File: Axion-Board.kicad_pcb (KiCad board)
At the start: 2 copper layers, 84 x 54.5 mm, 79 parts, among them J1 USB_C_Receptacle_USB2.0, J14 QE2B, J15 RGB2, J16 RGB1, J17 QE1, J18 QE2, J19 USB Header, J2 SWD, J20 PS2 Header, J21 QE2A, J3 QE1A, J4 QE1B, J6 GPIO, J7 GPIO, Q1 BSS138, Q10 BSS138, Q11 BSS138, Q2 BSS138, Q3 BSS138, Q4 BSS138, Q5 BSS138, Q6 BSS138, Q7 BSS138, Q8 BSS138, Q9 BSS138, SW1 SW_Push, U1 W25Q128JVS, U2 USBLC6-2SC6, U3 RP2040, U4 XC6206PxxxMR-Regulator_Linear, U5 SN74HCT125DR, U6 78M05_TO252-3, Y1 12MHz

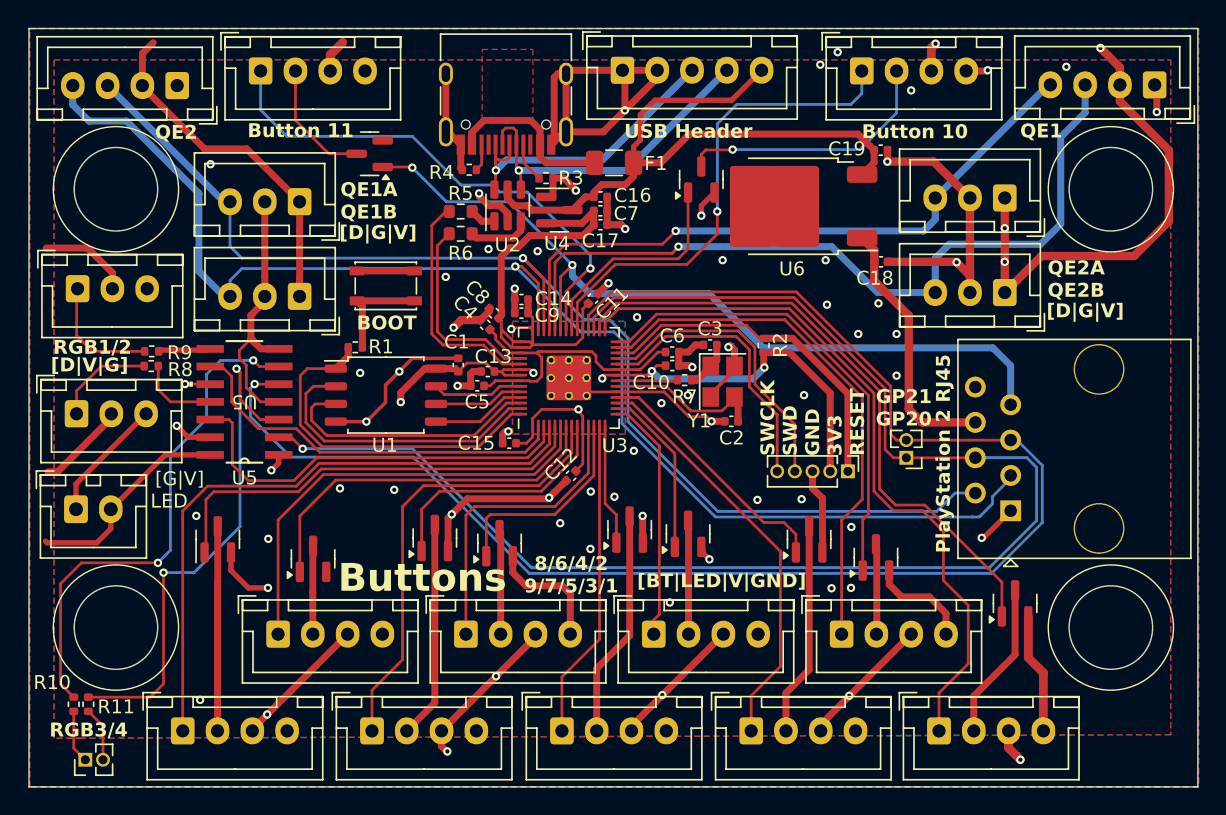
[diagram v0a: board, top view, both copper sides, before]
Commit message: Updated PCB
Changed Edge Cuts holes to mounting hole footprints, and updated track routing to avoid mounting hole courtyards
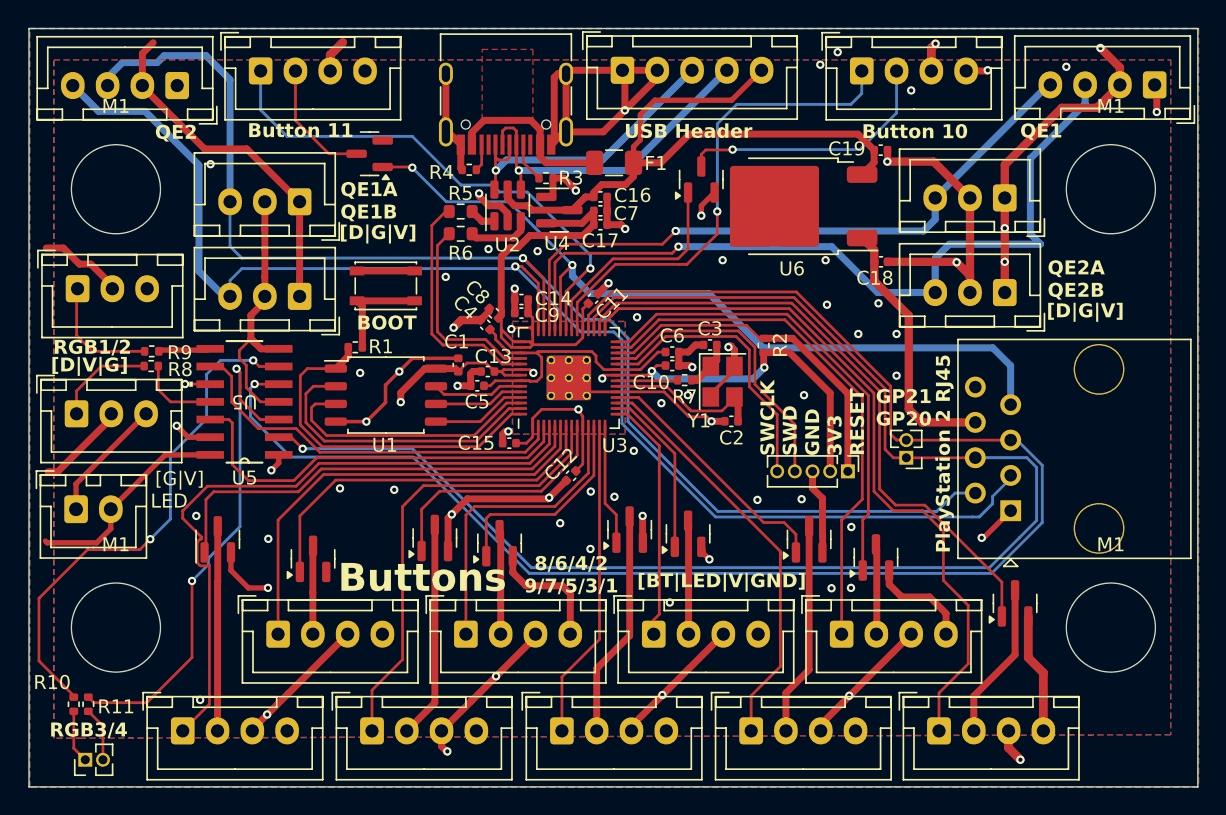
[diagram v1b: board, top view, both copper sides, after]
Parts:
- added M1: MountingHole_6.4mm_M6_ISO14580, MountingHole:MountingHole_6.4mm_M6_ISO14580, F.Cu at (177.7, 63.8)
- added M1: MountingHole_6.4mm_M6_ISO14580, MountingHole:MountingHole_6.4mm_M6_ISO14580, F.Cu at (177.7, 95.3)
- added M1: MountingHole_6.4mm_M6_ISO14580, MountingHole:MountingHole_6.4mm_M6_ISO14580, F.Cu at (106.2, 63.8)
- added M1: MountingHole_6.4mm_M6_ISO14580, MountingHole:MountingHole_6.4mm_M6_ISO14580, F.Cu at (106.2, 95.3)
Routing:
- net VBUS: track 148.9 -> 136.2 mm
- net /PS2CLK: track 86.9 -> 94.2 mm
- net /BT8: track 45.5 -> 47.8 mm
- net Net-(U5-1Y): track 37.8 -> 36.9 mm
- net /QE1A: track 57.4 -> 58.0 mm
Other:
- outline, holes or cut-outs redrawn
